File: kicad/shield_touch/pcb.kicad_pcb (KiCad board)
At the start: 2 copper layers, 37.6 x 35.1 mm, 22 parts, among them J1 Conn_01x12_Fem_l, J2 Conn_01x12_Fem_r, J3 Conn_01x09_Fem_b_l, J4 Conn_01x11_Fem_b_r_touch

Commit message: added throught via
- added throught via to increase GND contacts
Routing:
- net GND: track 54.8 -> 60.5 mm, vias 1 -> 2
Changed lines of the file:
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@@
     (thickness 1.6)
     (drawings 30)
-    (tracks 132)
+    (tracks 135)
     (zones 0)
     (modules 22)
@@
   (segment (start 107.696 77.47) (end 104.521 77.47) (width 0.25) (layer F.Cu) (net 1))
   (segment (start 104.521 77.47) (end 104.267 77.216) (width 0.25) (layer F.Cu) (net 1))
+  (segment (start 104.267 92.456) (end 107.442 92.456) (width 0.25) (layer F.Cu) (net 2) (status 400000))
+  (via (at 109.22 94.234) (size 0.6) (drill 0.4) (layers F.Cu B.Cu) (net 2))
+  (segment (start 107.442 92.456) (end 109.22 94.234) (width 0.25) (layer F.Cu) (net 2))
   (segment (start 110.236 84.328) (end 110.236 86.233) (width 0.25) (layer F.Cu) (net 2))
   (segment (start 111.76 92.456) (end 104.267 92.456) (width 0.25) (layer F.Cu) (net 2))

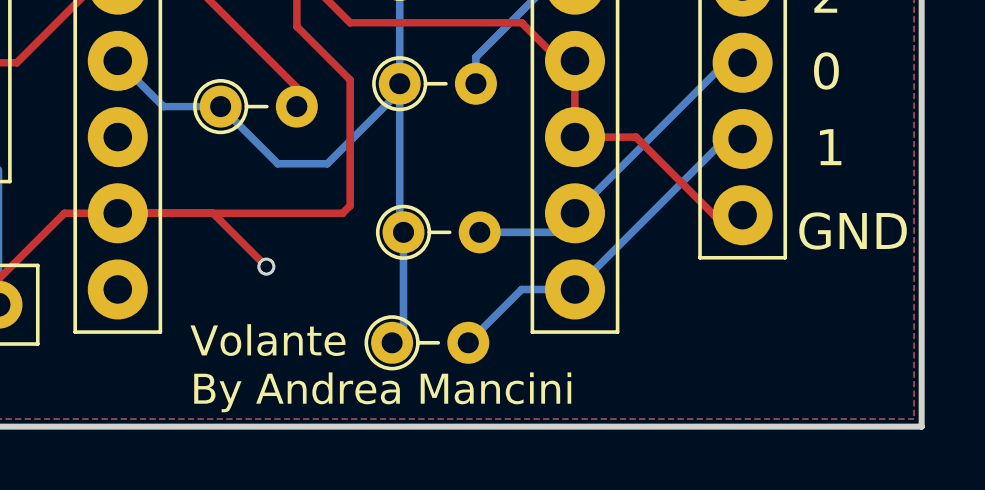
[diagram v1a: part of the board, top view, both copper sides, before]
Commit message: added logos
- open hw logo
- front back logos
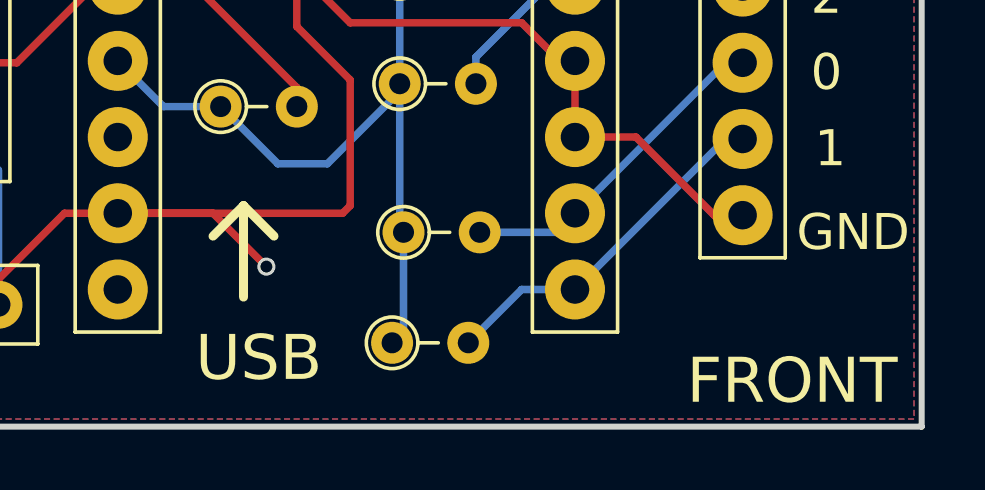
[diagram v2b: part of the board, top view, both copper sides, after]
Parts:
- added REF***: OSHW-Logo_5.7x6mm_SilkScreen, Symbols:OSHW-Logo_5.7x6mm_SilkScreen, B.Cu at (109.2, 95.0)
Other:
- board text added: "BACK"
- board text added: "FRONT"
- board text added: "USB"
- board text added: "Volante The GamePad By Andrea Mancini"
- board text removed: "Volante By Andrea Mancini"
